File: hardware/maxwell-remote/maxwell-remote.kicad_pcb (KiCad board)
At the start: 2 copper layers, 71.2 x 79 mm, 57 parts, among them J1 BOOT0, J10 CAN, J11 SPI1_C, J12 SPI1_B, J13 Display, J14 SPI1_A, J15 Left, J16 Right, J2 BOOT1, J3 ESPUART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

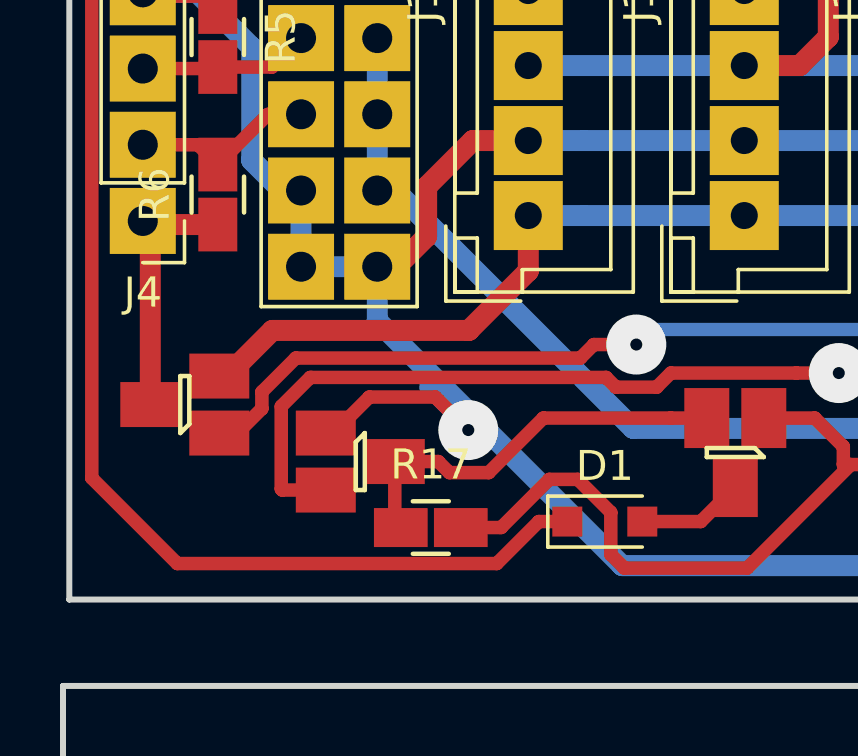
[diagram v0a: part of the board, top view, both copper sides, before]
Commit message: Maxwell Remote v2.0.3
* Fixes schematic such that an N-Channel mosfet is used for
  controlling the GND side of the SPI expansion ports.
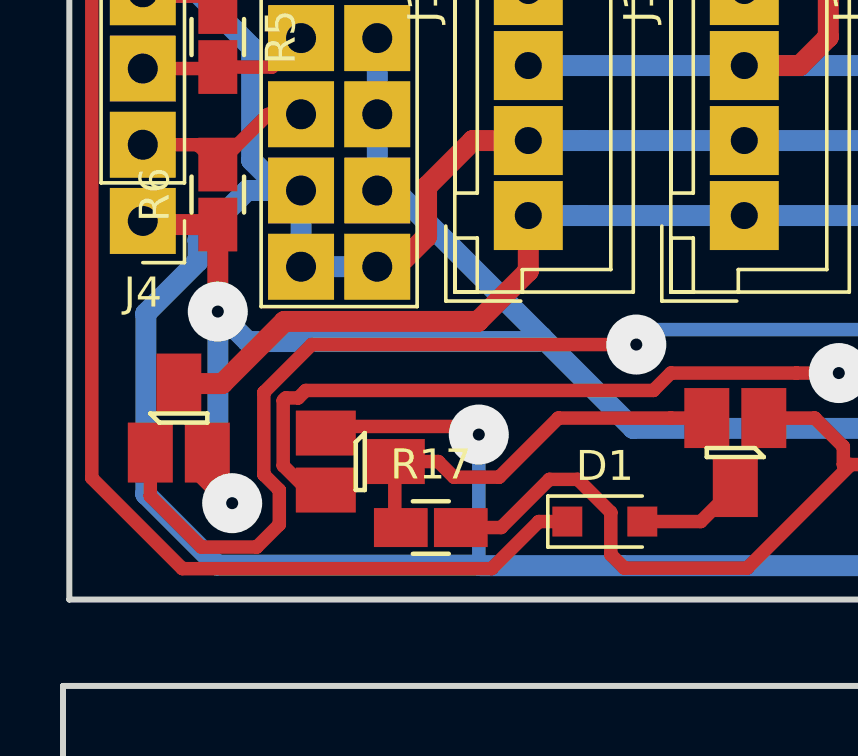
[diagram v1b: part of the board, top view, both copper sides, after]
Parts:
- Q5: value NTR1P02TI -> BSS138P
- moved Q5 0.49 mm to (113.7, 101.0), turned to 90 degrees
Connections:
- Q5 pad 2: Net-(J11-Pad1) -> GND_B
- Q5 pad 3: GND_B -> Net-(J11-Pad1)
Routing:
- net +3V3_B: track 180.5 -> 198.7 mm
- net GND_B: track 178.0 -> 194.8 mm, vias 1 -> 3
- net ESP_AVAILABLE_U: track 122.2 -> 131.2 mm
- net Net-(J11-Pad1): track 60.8 -> 62.3 mm
- net +3V3_U: track 73.1 -> 72.4 mm

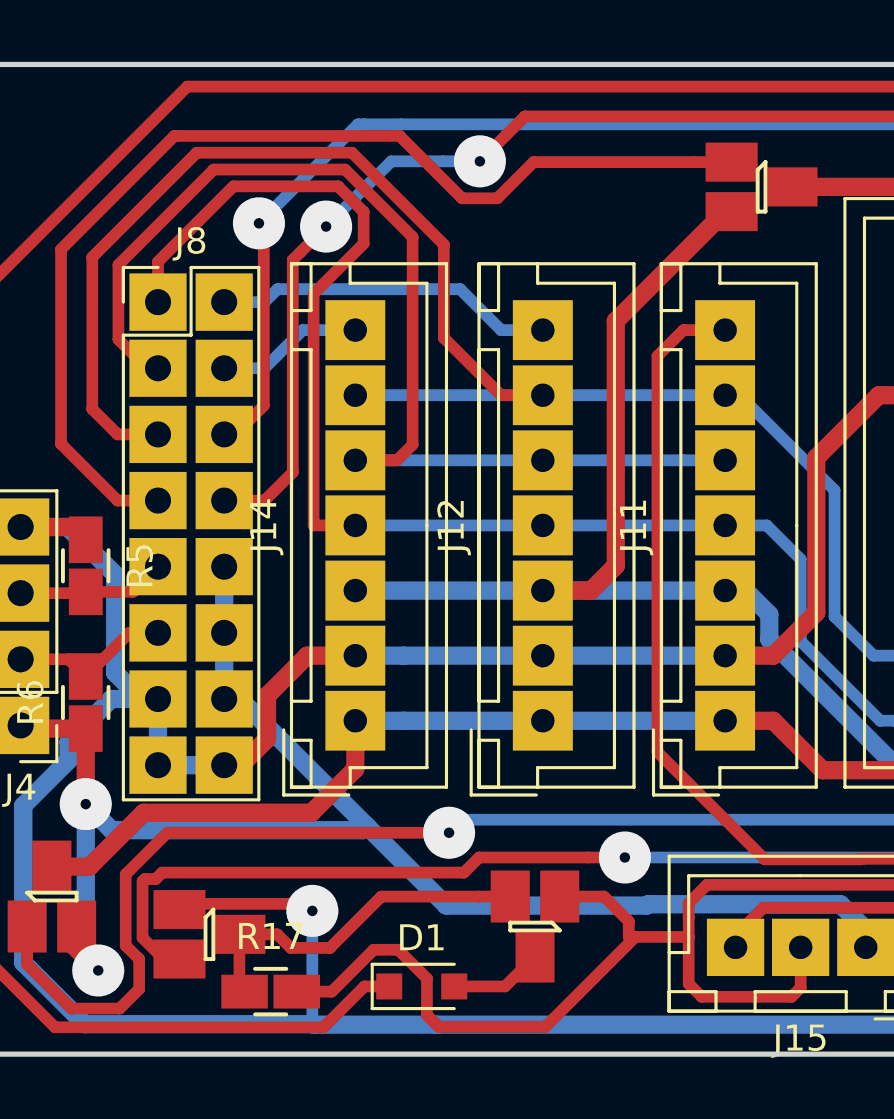
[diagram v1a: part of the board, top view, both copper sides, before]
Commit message: Fixing errata:
* Adding 10k pulldown for ENABLE_DISPLAY (backlight control).
* Adding 2u capacitor to PDOWN_PU to ensure WAKE is pulled high
  for long enough for the microcontroller to start.
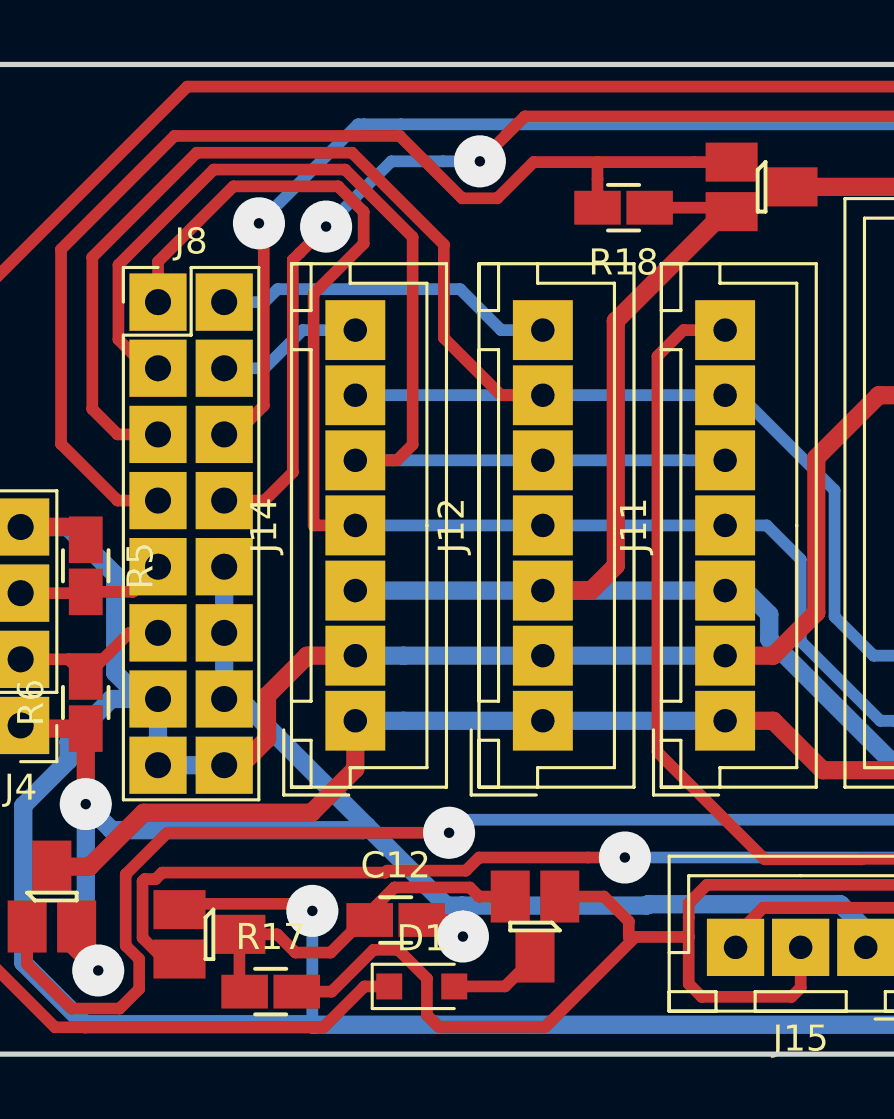
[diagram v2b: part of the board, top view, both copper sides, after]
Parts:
- added C12: 2u, coddingtonbear:0805_Milling, F.Cu at (126.8, 101.8)
- added R18: 10k, coddingtonbear:0805_Milling, F.Cu at (135.6, 74.5)
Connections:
- net Net-(Q3-Pad3) renamed /upper/PDOWN_PU
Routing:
- net +BATT: track 76.5 -> 79.7 mm
- net GND_B: track 194.8 -> 197.8 mm, vias 3 -> 4
- net ~ENABLE_SCREEN_U: track 41.2 -> 43.0 mm
- net /upper/PDOWN_PU: track 13.7 -> 14.3 mm

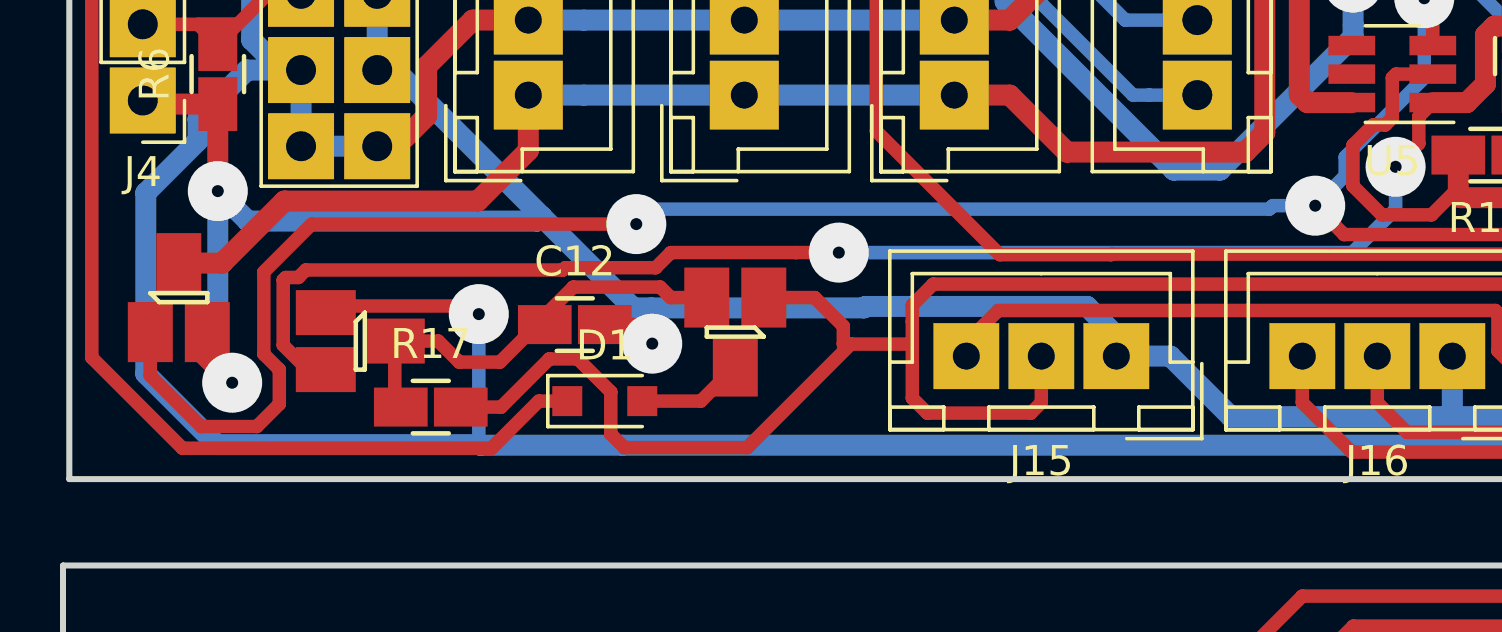
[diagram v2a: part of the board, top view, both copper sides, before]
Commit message: Fix: Removes weird pull-up-only-on-power-down for LEFT_A; instead just always pulls up LEFT_A.
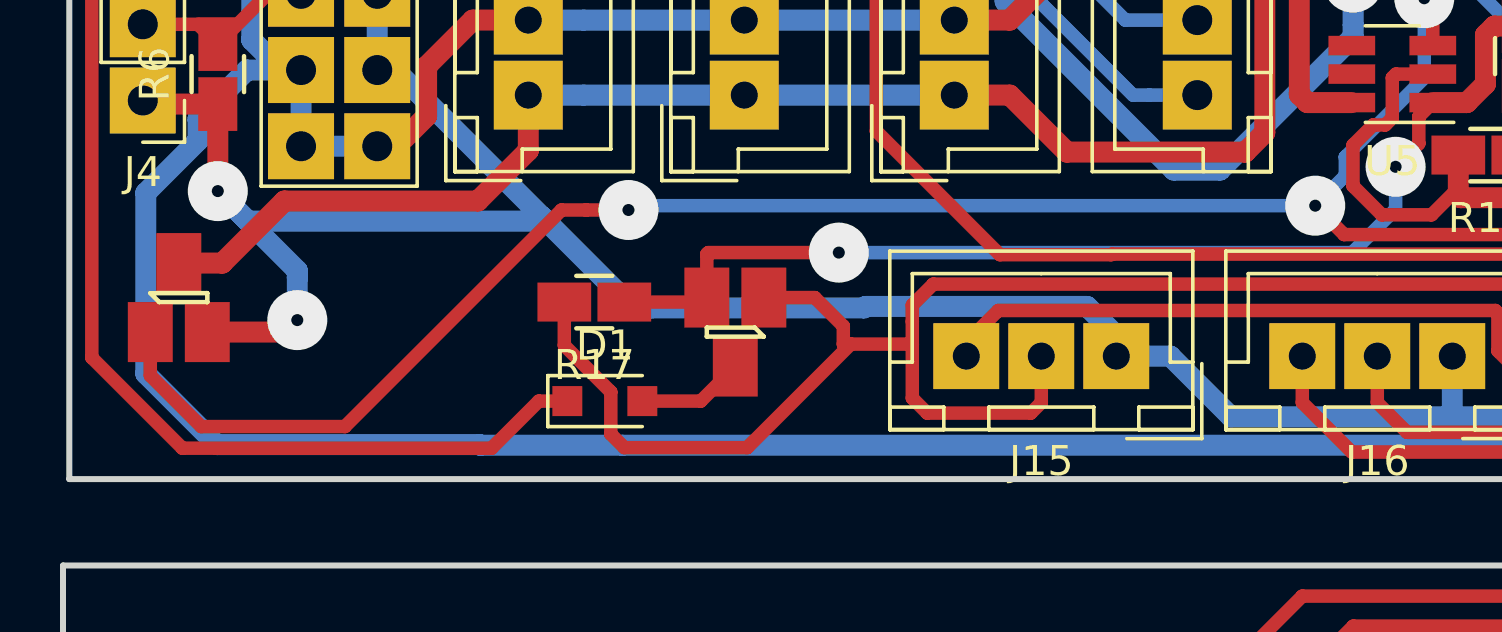
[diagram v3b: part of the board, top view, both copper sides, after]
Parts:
- removed C12: 2u, coddingtonbear:0805_Milling
- removed Q3: NTR1P02TI, coddingtonbear:SOT-23_LargePads
- moved R17 6.48 mm to (127.5, 101.1), turned to 180 degrees
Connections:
- Q4 pad 2: /upper/PDOWN_PU -> +3V3_U
- R17 pad 1: /upper/PDOWN_PU -> +3V3_U
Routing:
- net /upper/PDOWN_PU: track 14.3 -> 0.00 mm
- net +3V3_U: track 72.4 -> 58.2 mm
- net +3V3_B: track 198.7 -> 189.0 mm, vias 2 -> 1
- net ESP_AVAILABLE_U: track 131.2 -> 127.9 mm
- net GND_B: track 197.8 -> 194.6 mm, vias 4 -> 3
- net LEFT_A_U: track 56.9 -> 54.4 mm
